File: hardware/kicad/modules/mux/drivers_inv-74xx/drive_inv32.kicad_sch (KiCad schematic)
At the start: 8 parts, among them U299 74LS540, U300 74LS540, U301 74LS540, U302 74LS540

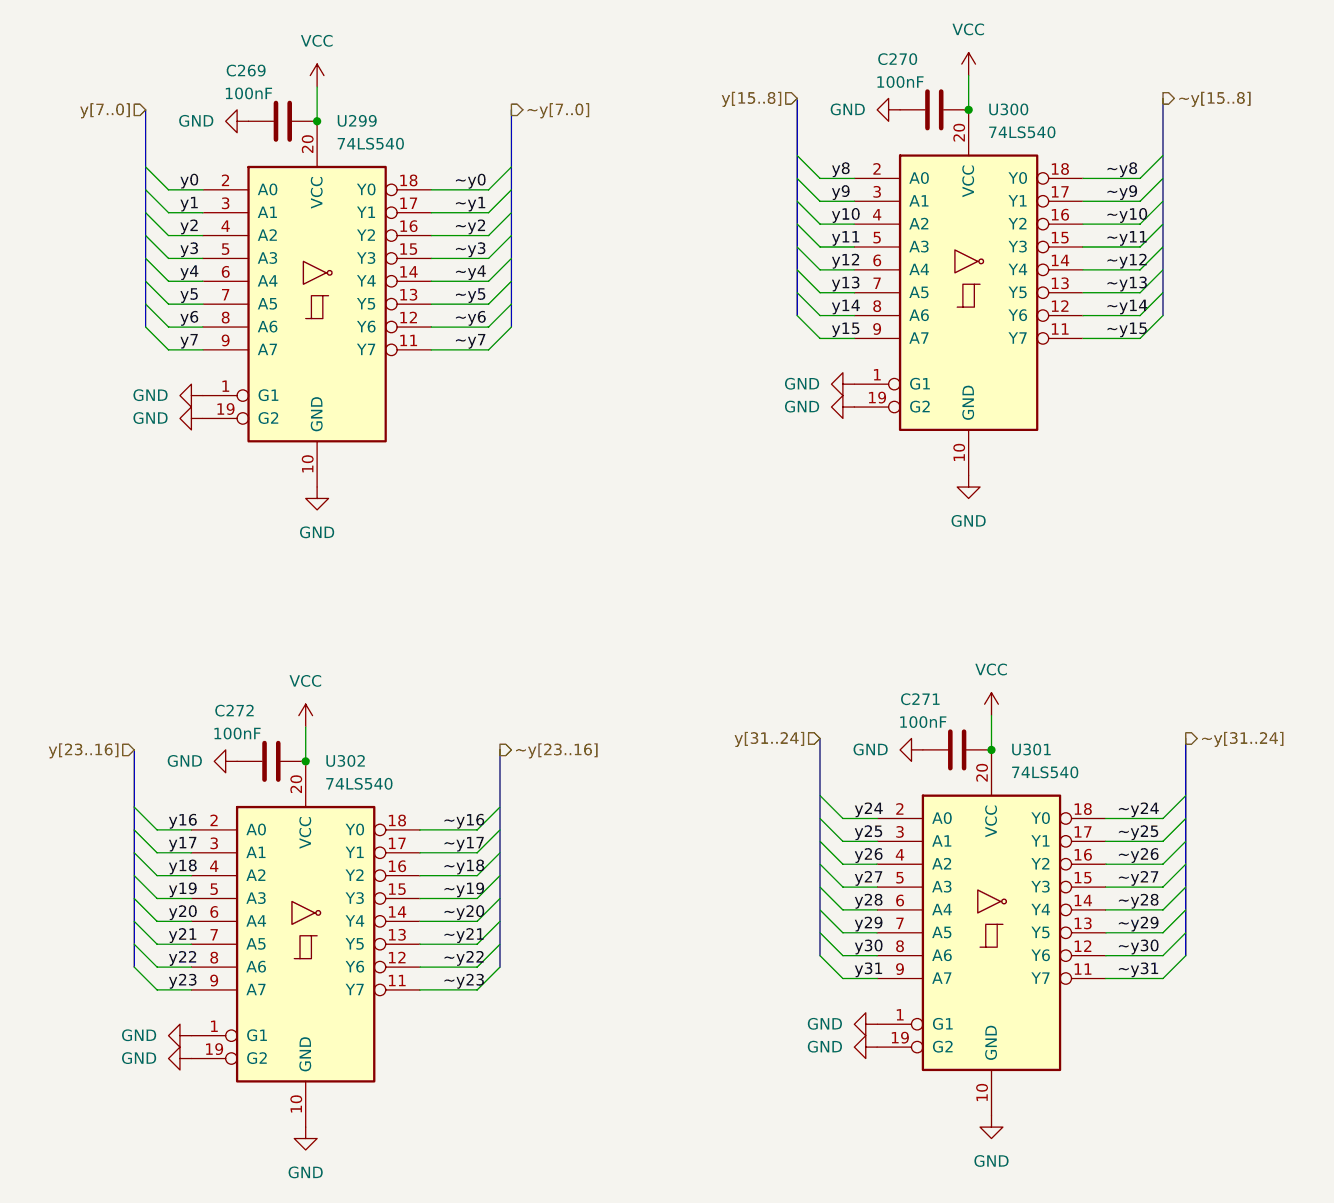
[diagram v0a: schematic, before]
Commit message: refactor: improved driver with data bus for readability
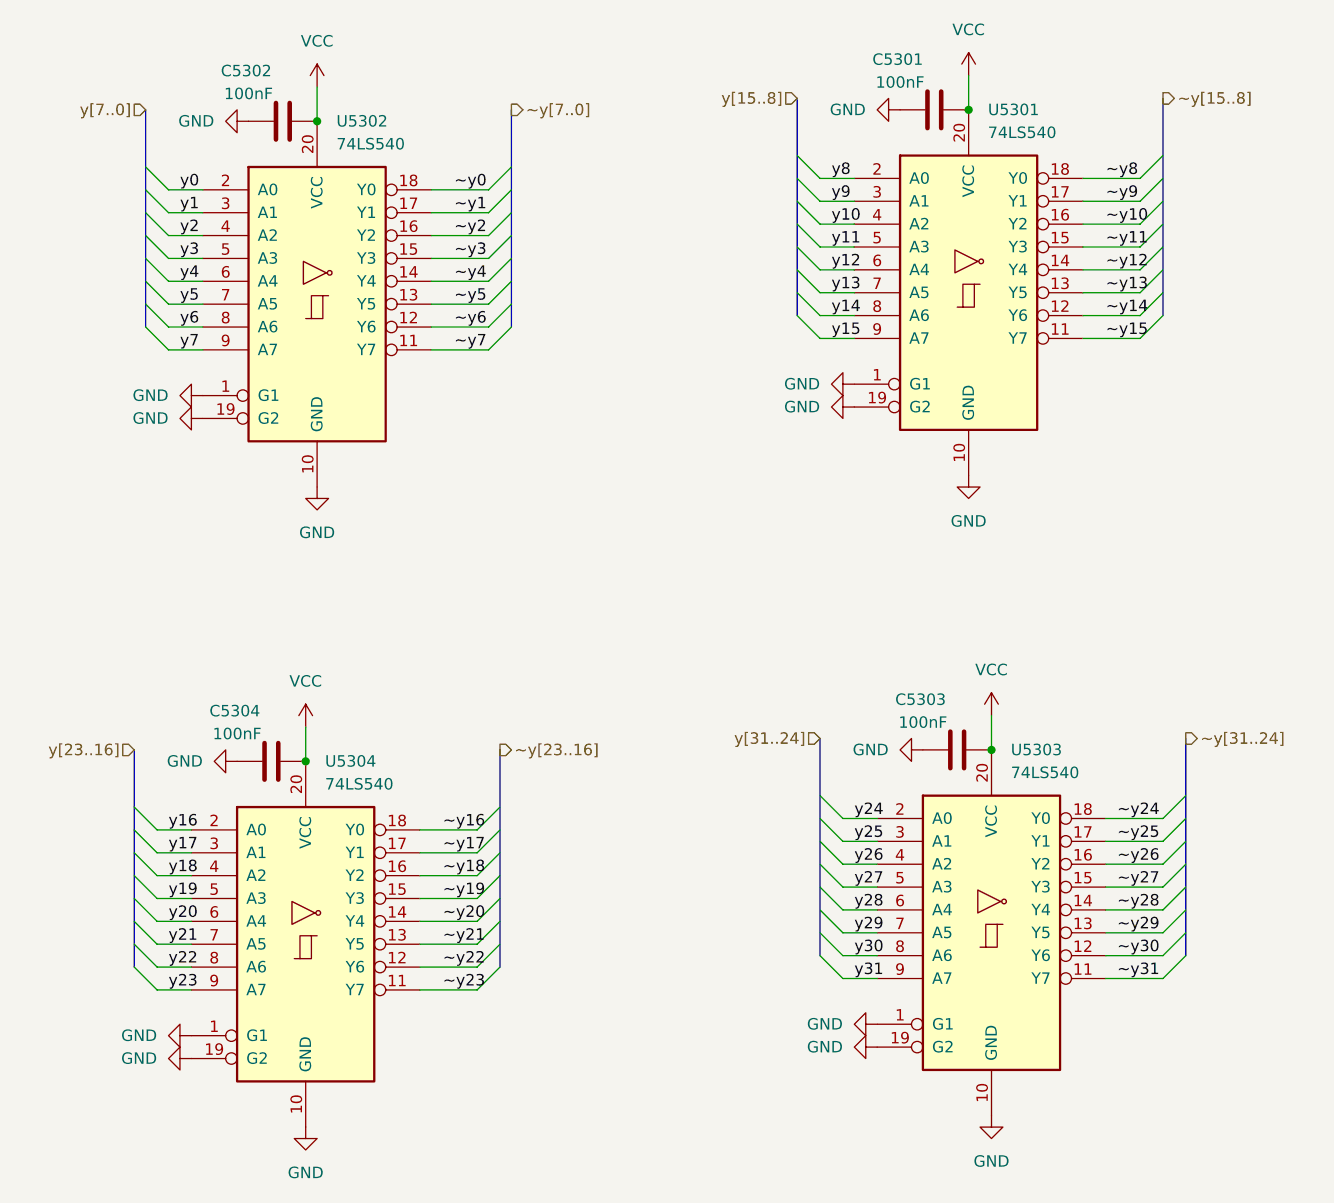
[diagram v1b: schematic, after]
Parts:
- renumbered C270 to C5301, C269 to C5302, C271 to C5303, C272 to C5304, U300 to U5301, U299 to U5302, U301 to U5303, U302 to U5304

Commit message: arch: added LEDs, override switches; fixed errors and warnings to 0
ready for routing after logical coherence check
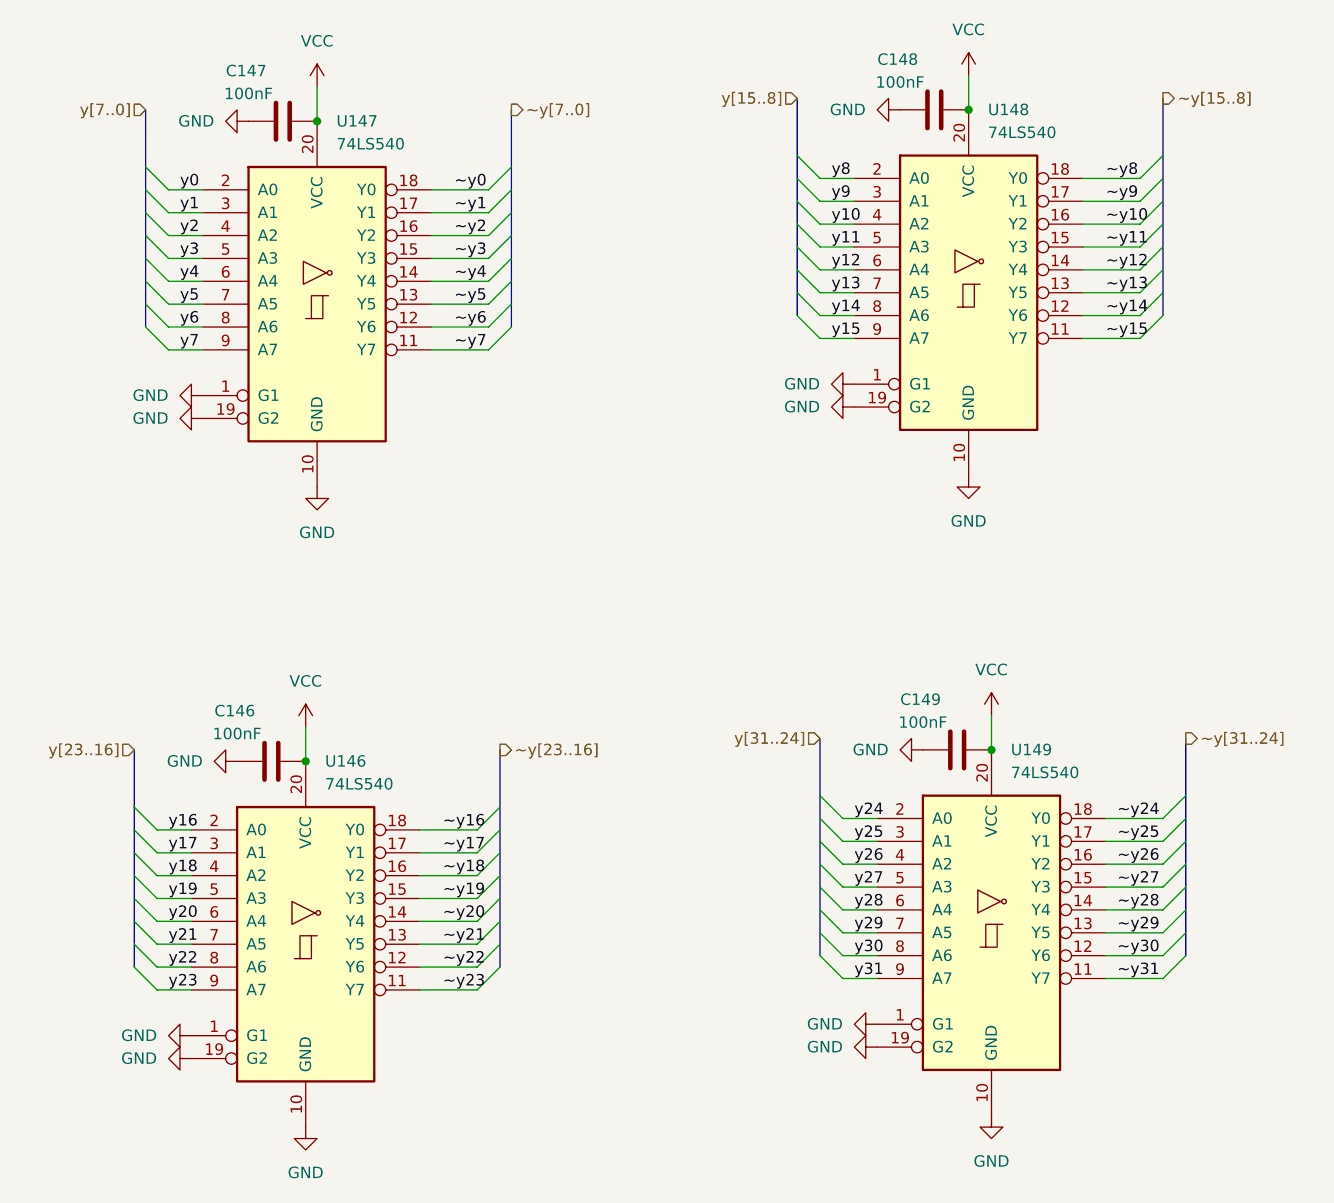
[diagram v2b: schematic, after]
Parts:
- renumbered C5304 to C146, C5302 to C147, C5301 to C148, C5303 to C149, U5304 to U146, U5302 to U147, U5301 to U148, U5303 to U149

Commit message: chore: modified muxes that alu depends on
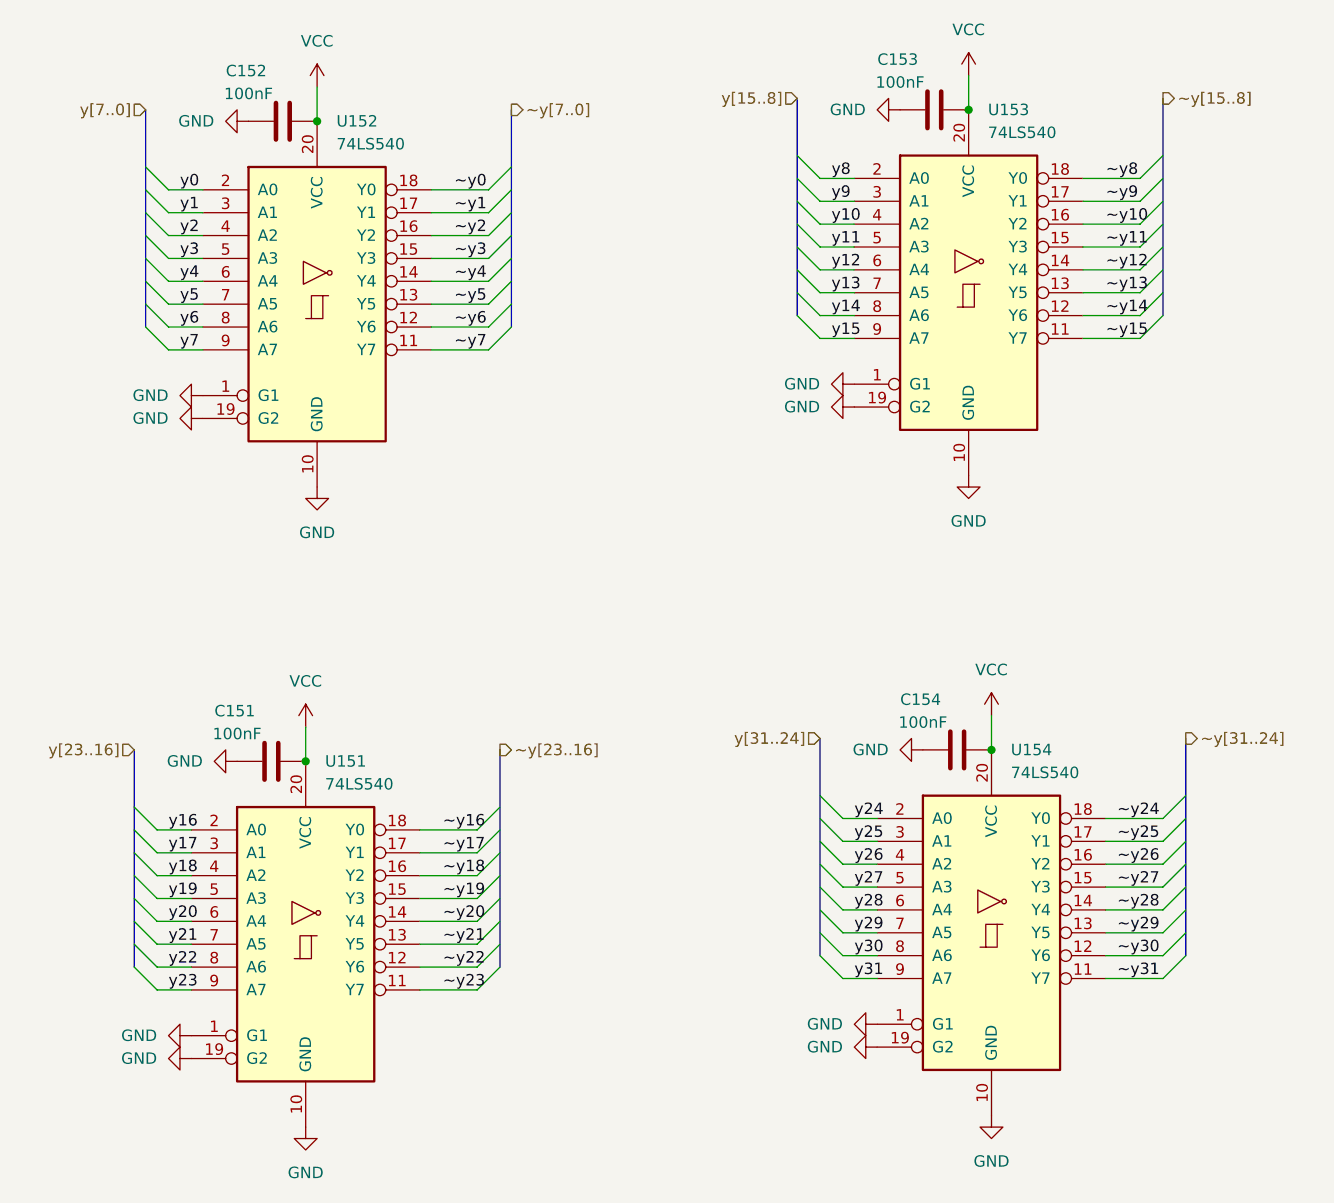
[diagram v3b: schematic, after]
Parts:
- renumbered C146 to C151, C147 to C152, C148 to C153, C149 to C154, U146 to U151, U147 to U152, U148 to U153, U149 to U154

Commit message: chore: power flag annotation on independent h-sheets
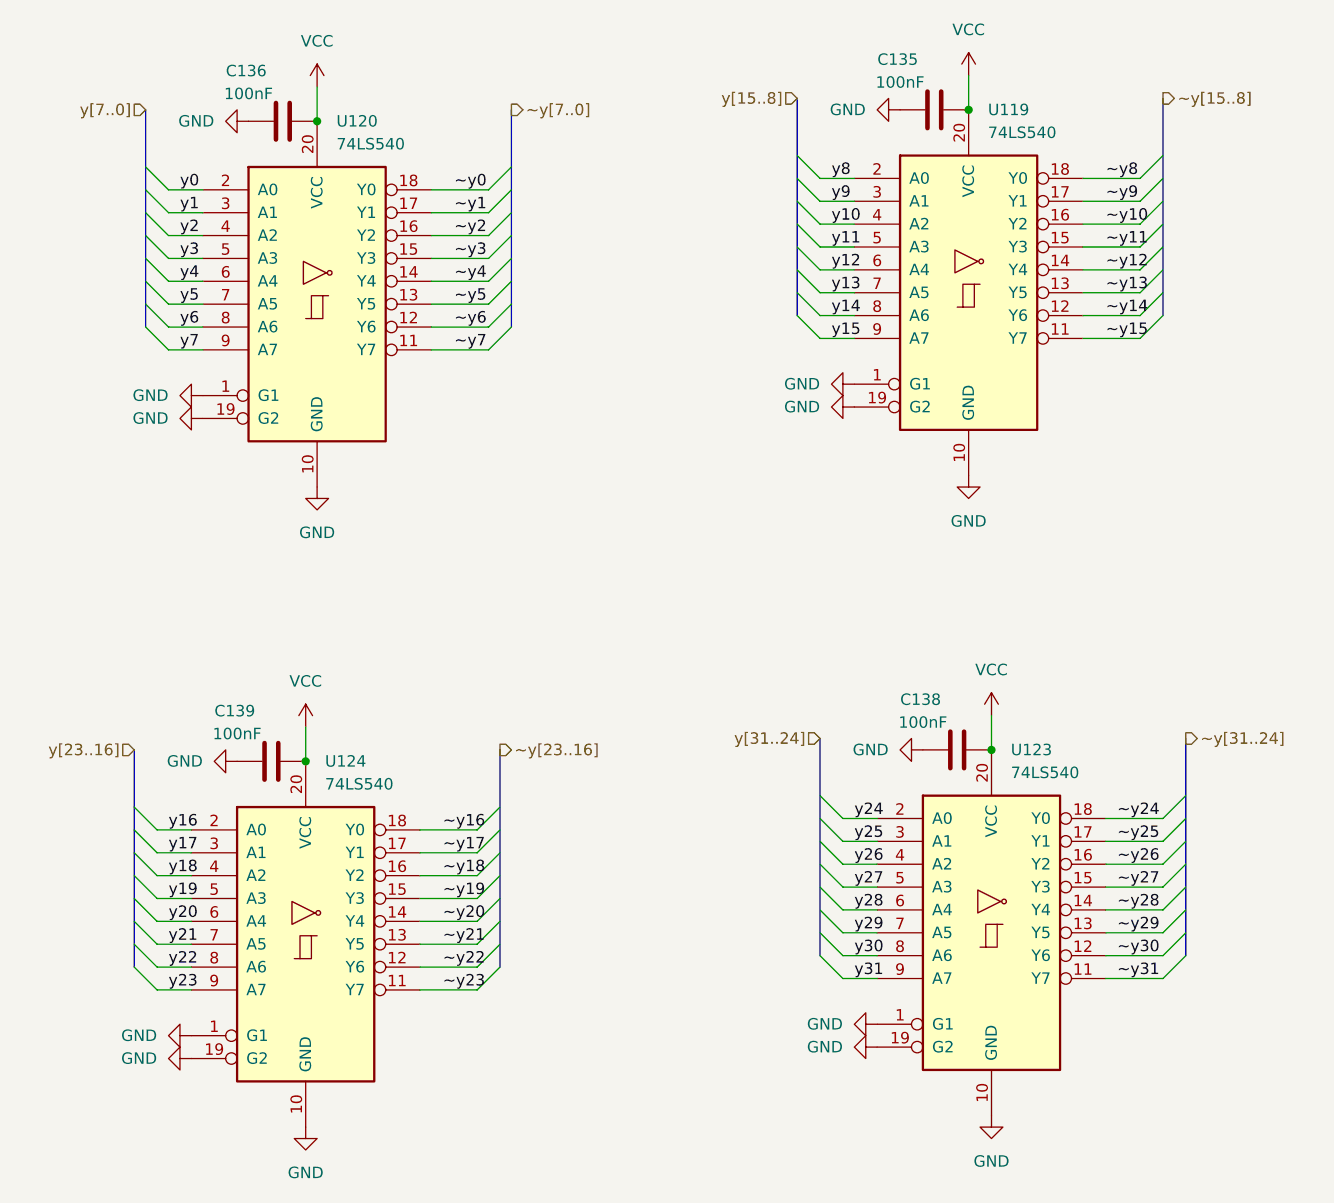
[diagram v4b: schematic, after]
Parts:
- renumbered C153 to C135, C152 to C136, C154 to C138, C151 to C139, U153 to U119, U152 to U120, U154 to U123, U151 to U124
